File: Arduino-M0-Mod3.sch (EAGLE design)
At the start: 111 parts, among them CN2 PINHEAD-2x5-P1.27, IC1 74LVC1G125DCKR, IC2 SAMD21G18A-AUT, IC3 MPM3610, IC4 MPM3810GQB-33, IC5 RTC_PCF8523T, IC6 EM4095, Y1 32.768kHz, Y4 32,768Khz

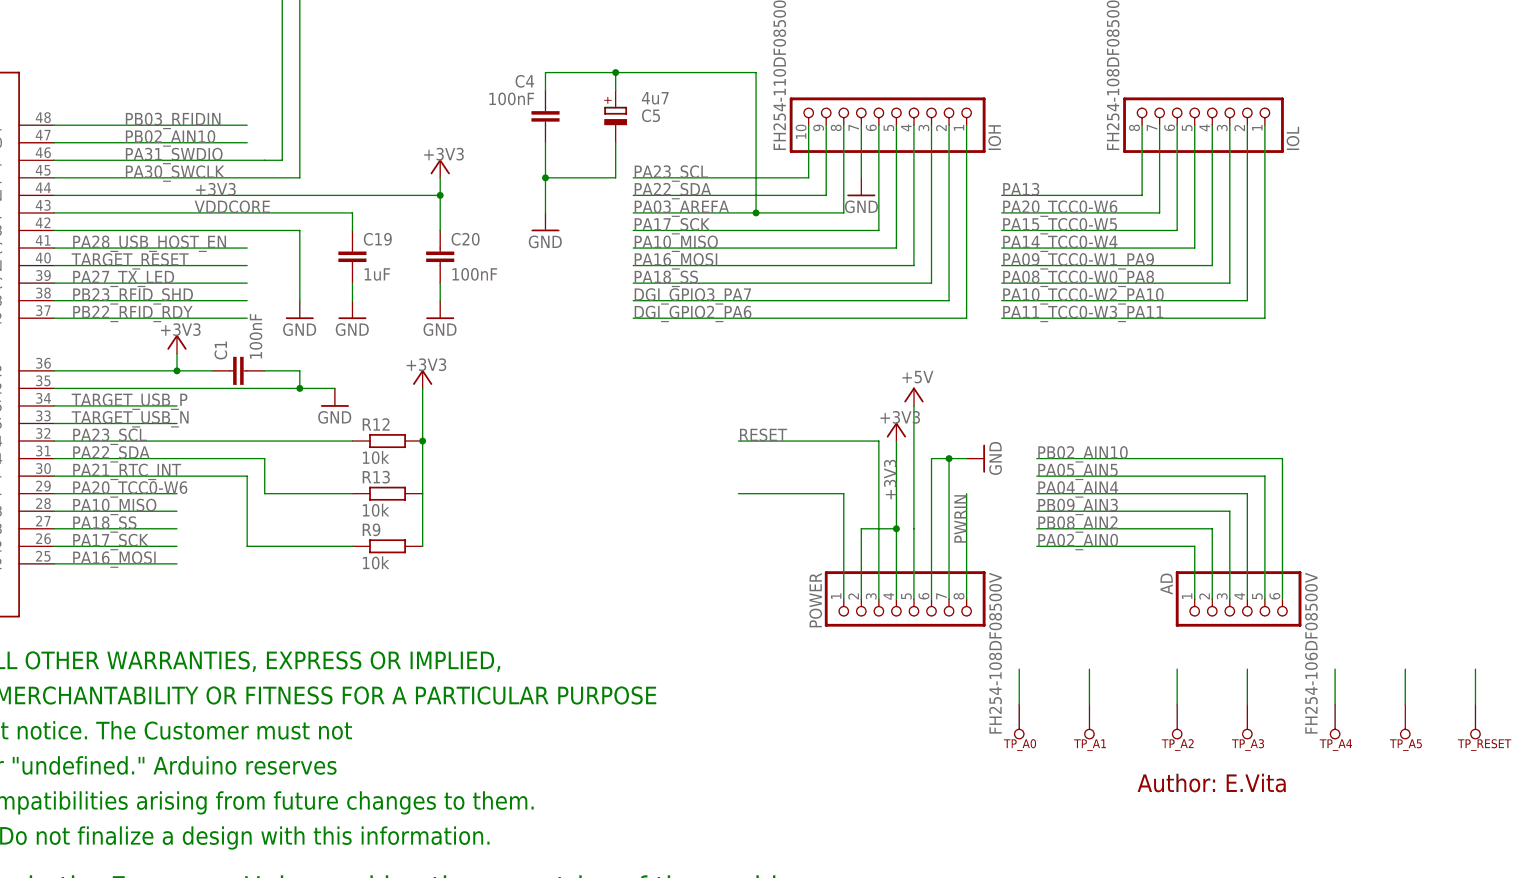
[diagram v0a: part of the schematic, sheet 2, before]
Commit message: Mod3 traces complete
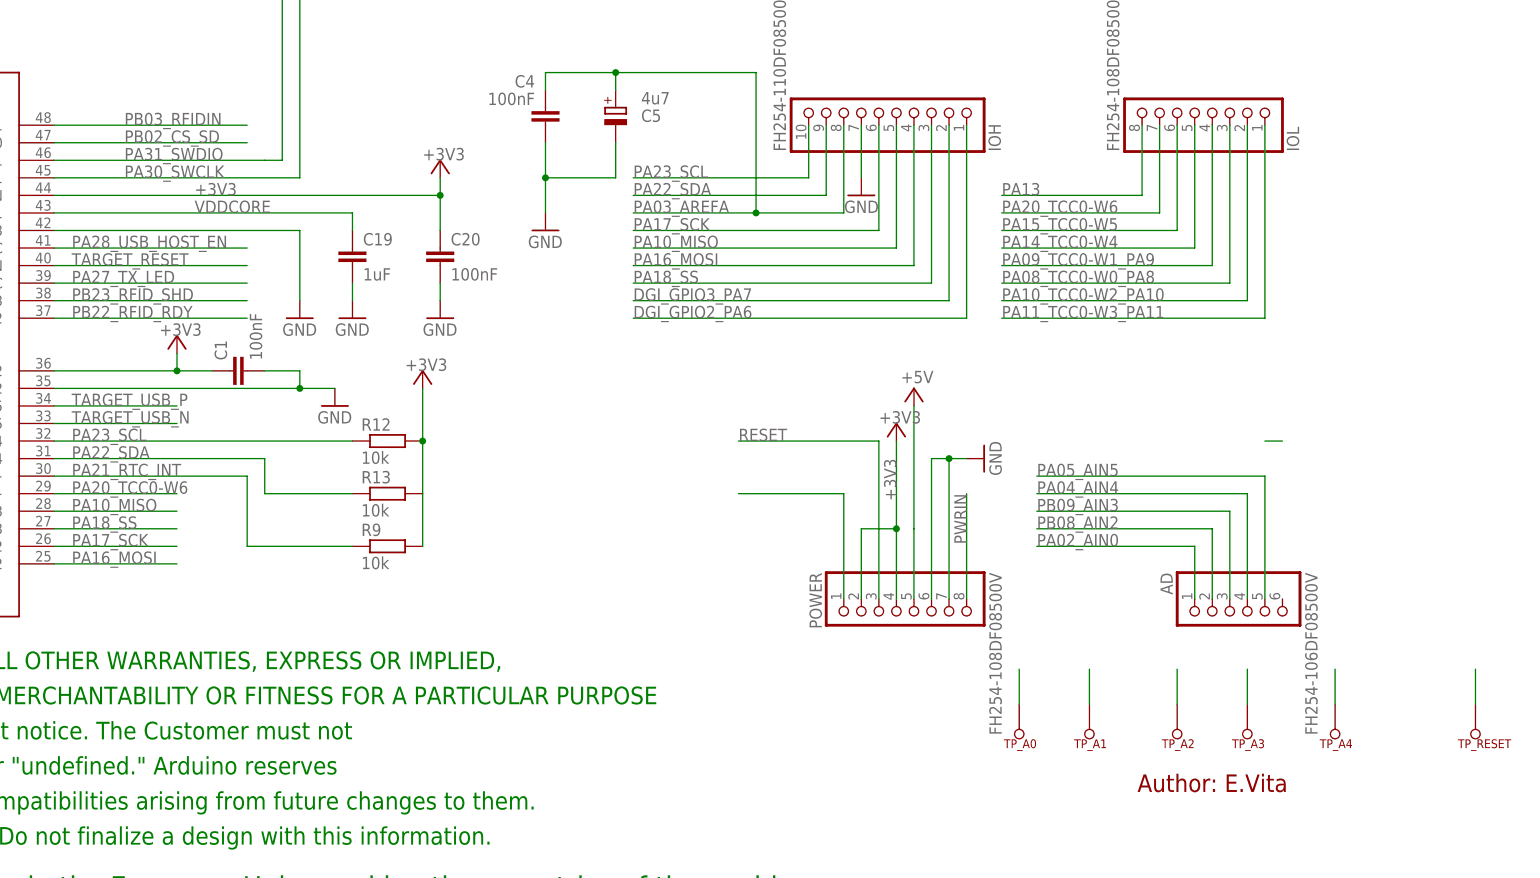
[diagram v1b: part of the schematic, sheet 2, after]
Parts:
- removed TP_A5: TP_SP, SmartPrj:TP_SP
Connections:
- removed net PB02_AIN10: AD.6, IC2.PB2/EIC/AIN10/SCOM5PAD0, TP_A5.TESTP
- removed net SD_CS: U$4.CS
- new net PB02_CS_SD: IC2.PB2/EIC/AIN10/SCOM5PAD0, U$4.CS
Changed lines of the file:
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@@
 <part name="TP_A3" library="SmartPrj" deviceset="TP_SP" device=""/>
 <part name="TP_A4" library="SmartPrj" deviceset="TP_SP" device=""/>
-<part name="TP_A5" library="SmartPrj" deviceset="TP_SP" device=""/>
 <part name="TP_0" library="SmartPrj" deviceset="TP_SP" device=""/>
 <part name="TP_1" library="SmartPrj" deviceset="TP_SP" device=""/>
@@
 </segment>
 </net>
-<net name="SD_CS" class="0">
+<net name="PB02_CS_SD" class="0">
 <segment>
 <wire x1="419.1" y1="20.32" x2="457.2" y2="20.32" width="0.1524" layer="91"/>
@@
 <instance part="TP_A3" gate="G$1" x="337.82" y="33.02" rot="R270"/>
 <instance part="TP_A4" gate="G$1" x="350.52" y="33.02" rot="R270"/>
-<instance part="TP_A5" gate="G$1" x="360.68" y="33.02" rot="R270"/>
 <instance part="TP_0" gate="G$1" x="375.92" y="149.86" rot="R90"/>
 <instance part="TP_1" gate="G$1" x="368.3" y="149.86" rot="R90"/>
@@
 <net name="PA05_AIN5" class="0">
 <segment>
+<pinref part="IC2" gate="G$1" pin="PA5/EIC/AIN5/SCOM0PAD1/TC0"/>
+<wire x1="76.2" y1="93.98" x2="43.18" y2="93.98" width="0.1524" layer="91"/>
+<label x="43.18" y="93.98" size="1.778" layer="95"/>
+</segment>
+<segment>
+<pinref part="TP_A4" gate="G$1" pin="TESTP"/>
+<wire x1="350.52" y1="33.02" x2="350.52" y2="38.1" width="0.1524" layer="91"/>
+</segment>
+<segment>
 <pinref part="AD" gate="A" pin="5"/>
 <wire x1="340.36" y1="48.26" x2="340.36" y2="66.04" width="0.1524" layer="91"/>
@@
 <label x="307.34" y="66.04" size="1.778" layer="95"/>
 </segment>
-<segment>
-<pinref part="IC2" gate="G$1" pin="PA5/EIC/AIN5/SCOM0PAD1/TC0"/>
-<wire x1="76.2" y1="93.98" x2="43.18" y2="93.98" width="0.1524" layer="91"/>
-<label x="43.18" y="93.98" size="1.778" layer="95"/>
-</segment>
-<segment>
-<pinref part="TP_A4" gate="G$1" pin="TESTP"/>
-<wire x1="350.52" y1="33.02" x2="350.52" y2="38.1" width="0.1524" layer="91"/>
-</segment>
 </net>
 <net name="PA08_TCC0-W0_PA8" class="0">
@@
 </segment>
 </net>
-<net name="PB02_AIN10" class="0">
-<segment>
-<pinref part="AD" gate="A" pin="6"/>
-<wire x1="342.9" y1="48.26" x2="342.9" y2="68.58" width="0.1524" layer="91"/>
-<wire x1="342.9" y1="68.58" x2="307.34" y2="68.58" width="0.1524" layer="91"/>
-<label x="307.34" y="68.58" size="1.778" layer="95"/>
-</segment>
+<net name="PB02_CS_SD" class="0">
 <segment>
 <pinref part="IC2" gate="G$1" pin="PB2/EIC/AIN10/SCOM5PAD0"/>
 <wire x1="165.1" y1="114.3" x2="193.04" y2="114.3" width="0.1524" layer="91"/>
 <label x="175.26" y="114.3" size="1.778" layer="95"/>
-</segment>
-<segment>
-<pinref part="TP_A5" gate="G$1" pin="TESTP"/>
-<wire x1="360.68" y1="33.02" x2="360.68" y2="38.1" width="0.1524" layer="91"/>
 </segment>
 </net>
@@
 </segment>
 </net>
+<net name="N$15" class="0">
+<segment>
+<wire x1="342.9" y1="71.12" x2="340.36" y2="71.12" width="0.1524" layer="91"/>
+</segment>
+</net>
